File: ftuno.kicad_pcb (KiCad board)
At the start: 2 copper layers, 68.6 x 53.3 mm, 57 parts, among them CN1 AFC10-S04QCA-00, J1 USB_C_Receptacle_USB2.0_16P, J10 Conn_01x10_Socket, J11 Conn_01x08_Pin, J12 Conn_01x08_Socket, J13 DC050-T, J2 Conn_02x03_Odd_Even, J3 Conn_01x08_Pin, J4 Conn_01x08_Socket, J5 Conn_02x04_Odd_Even, J6 Conn_01x06_Pin, J7 Conn_01x06_Socket, J8 Conn_01x04_Socket, J9 Conn_01x10_Pin, Q1 AO3401, Q2 BSS138PS_C5224289, Q3 BSS138PS_C5224289, SW1 SK12D07VG4, SW2 SKHMQLE010, U1 CH340C, U2 SPX1117M3-L-5-0, U3 ME6217C33M5G, U4 ATmega328P-A, X1 CSTCE16M0V53-R0

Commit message: silkscreen rework
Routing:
- net +5V: track 185.9 -> 184.9 mm
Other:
- board text added: "6.3~19V DC IN"
- board text added: "ESD Safe"
- board text added: "ON<->OFF"
- board text added: "Reset"
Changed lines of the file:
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@@
 		(tags "capacitor")
 		(property "Reference" "C3"
-			(at -1.6386 0.0254 0)
+			(at 2.584 0.0762 0)
 			(layer "F.SilkS")
 			(effects
@@
 		(tags "capacitor")
 		(property "Reference" "C9"
-			(at -1.5748 -0.0254 0)
+			(at 0.6305 -0.883 0)
 			(layer "F.SilkS")
 			(effects
@@
 		(at 81.407 70.358 -90)
 		(property "Reference" "U3"
-			(at 0 2.0066 90)
+			(at 0 -2.1545 90)
 			(layer "F.SilkS")
 			(effects
@@
 		)
 	)
+	(gr_text "6.3~19V\nDC IN"
+		(at 91.1815 88.525 0)
+		(layer "F.SilkS")
+		(effects
+			(font
+				(size 0.8 0.8)
+				(thickness 0.1)
+			)
+			(justify left)
+		)
+	)
 	(gr_text "GND"
-		(at 99.314 44.1452 90)
+		(at 99.314 44.196 90)
 		(layer "F.SilkS" knockout)
 		(effects
@@
 	)
 	(gr_text "5V"
-		(at 103.378 84.4804 90)
+		(at 103.3735 84.582 90)
 		(layer "F.SilkS")
 		(effects
@@
 	)
 	(gr_text "3V3"
-		(at 108.712 84.5312 90)
+		(at 108.712 84.582 90)
 		(layer "F.SilkS")
 		(effects
@@
 		)
 	)
+	(gr_text "ESD Safe"
+		(at 86.2285 52.838 90)
+		(layer "F.SilkS")
+		(effects
+			(font
+				(size 0.8 0.8)
+				(thickness 0.1)
+			)
+		)
+	)
 	(gr_text "VIN\n"
-		(at 118.8212 84.5312 90)
+		(at 118.8212 84.582 90)
 		(layer "F.SilkS")
 		(effects
@@
 		)
 	)
+	(gr_text "ON<->OFF"
+		(at 78.3545 70.745 90)
+		(layer "F.SilkS")
+		(effects
+			(font
+				(size 0.8 0.8)
+				(thickness 0.1)
+			)
+		)
+	)
 	(gr_text "GND"
-		(at 114.808 84.582 90)
+		(at 114.8035 84.582 90)
 		(layer "F.SilkS" knockout)
 		(effects
@@
 	)
 	(gr_text "D12"
-		(at 104.424 44.129 90)
+		(at 104.424 44.196 90)
 		(layer "F.SilkS")
 		(effects
@@
 	)
 	(gr_text "D7"
-		(at 118.618 44.129 90)
+		(at 118.618 44.196 90)
 		(layer "F.SilkS")
 		(effects
@@
 	)
 	(gr_text "5V"
-		(at 111.0488 84.5312 90)
+		(at 111.0488 84.582 90)
 		(layer "F.SilkS")
 		(effects
@@
 	)
 	(gr_text "SCL"
-		(at 91.694 44.129 90)
+		(at 91.694 44.196 90)
 		(layer "F.SilkS")
 		(effects
@@
 		)
 	)
+	(gr_text "Reset"
+		(at 78.4815 45.853 0)
+		(layer "F.SilkS")
+		(effects
+			(font
+				(size 0.8 0.8)
+				(thickness 0.1)
+			)
+		)
+	)
 	(gr_text "D4"
 		(at 126.238 44.196 90)
@@
 	)
 	(via
-		(at 93.472 67.056)
+		(at 92.4515 66.046)
 		(size 0.61)
 		(drill 0.305)
@@
 	)
 	(segment
-		(start 88.046 77.013)
-		(end 88.046 78.5255)
-		(width 0.8)
+		(start 95.377 63.754)
+		(end 95.377 64.7715)
+		(width 0.5)
 		(layer "F.Cu")
 		(net 7)
 	)
 	(segment
-		(start 95.377 66.5988)
-		(end 93.4038 68.572)
-		(width 0.5)
+		(start 88.046 77.013)
+		(end 88.046 78.5255)
+		(width 0.8)
 		(layer "F.Cu")
 		(net 7)
@@
 	)
 	(segment
-		(start 93.4038 68.572)
-		(end 88.466 68.572)
-		(width 0.5)
-		(layer "F.Cu")
-		(net 7)
-	)
-	(segment
 		(start 134.131 57.004)
 		(end 134.131 56.204)
@@
 	)
 	(segment
-		(start 95.377 63.754)
-		(end 95.377 66.5988)
-		(width 0.5)
-		(layer "F.Cu")
-		(net 7)
-	)
-	(segment
 		(start 129.328 73.974979)
 		(end 129.328 73.237)
@@
 	)
 	(segment
+		(start 95.377 64.7715)
+		(end 91.5765 68.572)
+		(width 0.5)
+		(layer "F.Cu")
+		(net 7)
+	)
+	(segment
 		(start 133.381 59.204)
 		(end 137.743 59.204)
@@
 	)
 	(segment
+		(start 91.5765 68.572)
+		(end 88.466 68.572)
+		(width 0.5)
+		(layer "F.Cu")
+		(net 7)
+	)
+	(segment
 		(start 112.59 69.12)
 		(end 113.665 69.12)
@@
 	)
 	(segment
-		(start 97.028 60.452)
-		(end 95.8088 59.2328)
-		(width 0.6)
-		(layer "F.Cu")
-		(net 24)
-	)
-	(segment
-		(start 94.8483 59.2328)
-		(end 93.3025 57.687)
+		(start 95.8088 59.2328)
+		(end 94.8483 59.2328)
 		(width 0.6)
 		(layer "F.Cu")
@@
 	)
 	(segment
-		(start 95.8088 59.2328)
-		(end 94.8483 59.2328)
+		(start 94.8483 59.2328)
+		(end 93.3025 57.687)
+		(width 0.6)
+		(layer "F.Cu")
+		(net 24)
+	)
+	(segment
+		(start 96.33025 59.75425)
+		(end 95.8088 59.2328)
 		(width 0.6)
 		(layer "F.Cu")
@@
 	)
 	(via
-		(at 97.028 60.452)
+		(at 96.33025 59.75425)
 		(size 0.61)
 		(drill 0.305)
@@
 	)
 	(segment
-		(start 97.028 60.452)
-		(end 97.028 65.908442)
+		(start 110.447 68.115)
+		(end 110.49 68.072)
 		(width 0.6)
 		(layer "B.Cu")
@@
 	)
 	(segment
+		(start 96.33025 59.75425)
+		(end 97.028 60.452)
+		(width 0.6)
+		(layer "B.Cu")
+		(net 24)
+	)
+	(segment
 		(start 120.396 55.626)
 		(end 114.681 55.626)
@@
 	)
 	(segment
-		(start 97.028 65.908442)
-		(end 99.234558 68.115)
-		(width 0.6)
-		(layer "B.Cu")
-		(net 24)
-	)
-	(segment
 		(start 101.854 42.799)
 		(end 101.854 40.259)
@@
 	)
 	(segment
-		(start 110.447 68.115)
-		(end 110.49 68.072)
+		(start 97.028 65.908442)
+		(end 99.234558 68.115)
 		(width 0.6)
 		(layer "B.Cu")
@@
 	)
 	(segment
+		(start 97.028 60.452)
+		(end 97.028 65.908442)
+		(width 0.6)
+		(layer "B.Cu")
+		(net 24)
+	)
+	(segment
 		(start 128.6645 60.585)
 		(end 126.7535 58.674)
@@
 	)
 	(segment
+		(start 125.449 43.588)
+		(end 126.238 42.799)
+		(width 0.4)
+		(layer "F.Cu")
+		(net 33)
+	)
+	(segment
 		(start 121.09 73.12)
 		(end 124.013675 73.12)
@@
 	)
 	(segment
-		(start 125.449 43.588)
-		(end 126.238 42.799)
-		(width 0.4)
-		(layer "F.Cu")
-		(net 33)
-	)
-	(segment
 		(start 126.238 42.799)
 		(end 126.238 40.259)
@@
 		(filled_areas_thickness no)
 		(fill yes
-			(thermal_gap 0.5)
+			(thermal_gap 0.25)
 			(thermal_bridge_width 0.5)
 		)

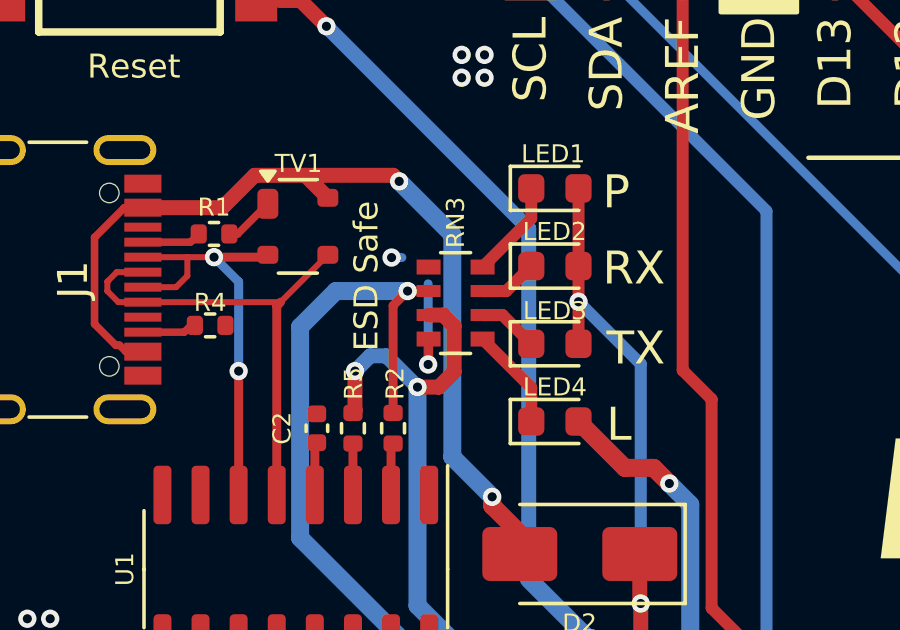
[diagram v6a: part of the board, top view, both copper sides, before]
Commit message: use seperate resistors for led, use higher rns for level shifters
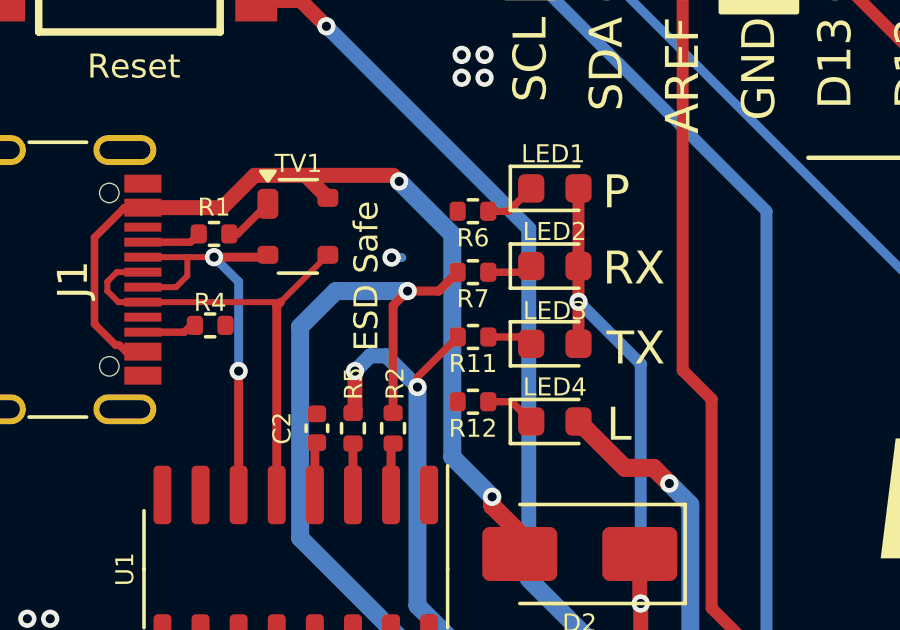
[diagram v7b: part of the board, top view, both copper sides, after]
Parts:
- removed RN3: 2.2k, Resistor_SMD:R_Array_Convex_4x0603
- added R11: 2.2k, Resistor_SMD:R_0402_1005Metric, F.Cu at (89.8, 54.9)
- added R12: 2.2k, Resistor_SMD:R_0402_1005Metric, F.Cu at (89.8, 57.0)
- added R6: 2.2k, Resistor_SMD:R_0402_1005Metric, F.Cu at (89.8, 50.7)
- added R7: 2.2k, Resistor_SMD:R_0402_1005Metric, F.Cu at (89.8, 52.7)
- RN1, RN2: value 2.2k -> 4.7k
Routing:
- net GND: track 22.2 -> 18.6 mm, vias 33 -> 32
- net TX1: track 90.8 -> 89.1 mm
- net Net-(LED4-K): track 3.42 -> 1.71 mm
- net Net-(LED1-K): track 3.29 -> 1.75 mm
- net RX0: track 97.3 -> 98.5 mm
